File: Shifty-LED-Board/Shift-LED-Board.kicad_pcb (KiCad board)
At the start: 2 copper layers, 80 x 30 mm, 51 parts, among them U1 74AHCT595, U2 74AHCT595, U3 74AHCT595

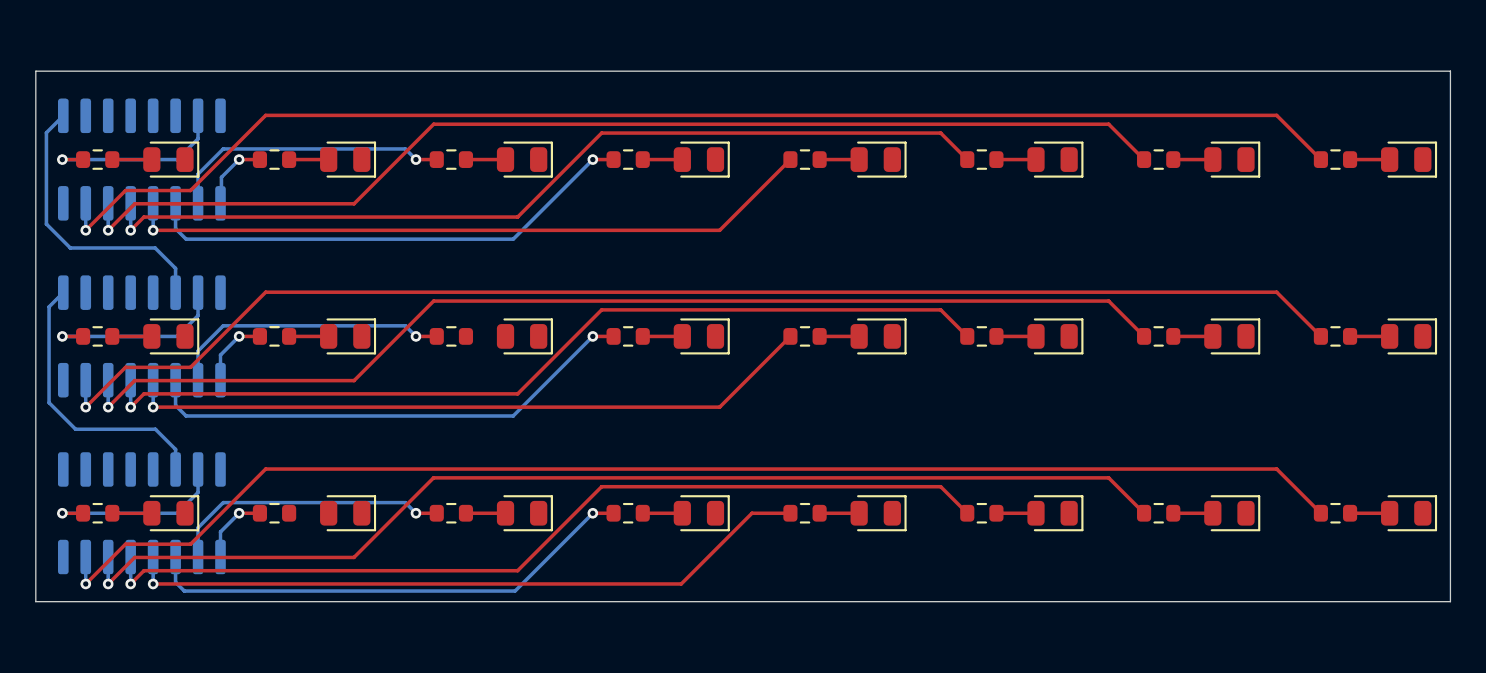
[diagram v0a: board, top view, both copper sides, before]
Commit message: added data routes on shfity board
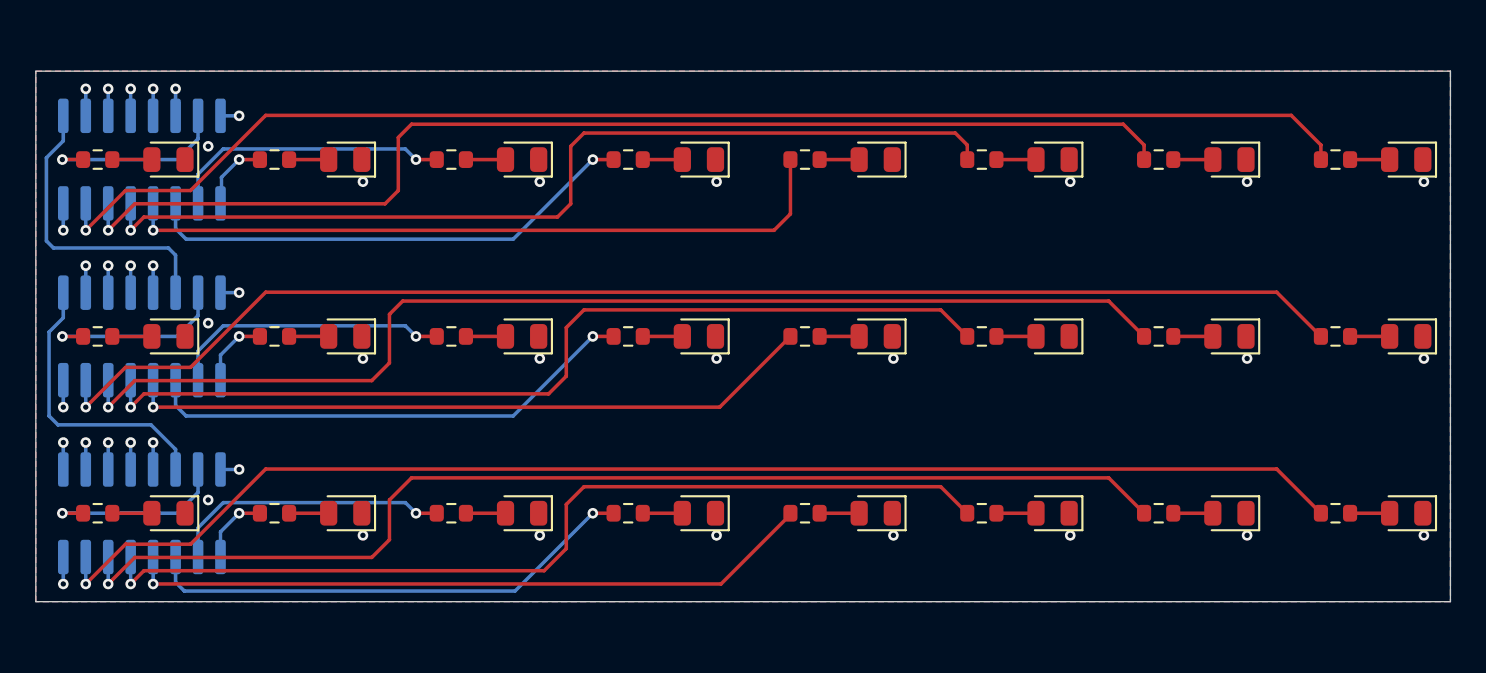
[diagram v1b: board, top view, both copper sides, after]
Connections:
- net /SER1 renamed /SER_IN
- U1 pad 10: unconnected-(U1-~{SRCLR}-Pad10) -> /SR_CLR
- U2 pad 10: unconnected-(U2-~{SRCLR}-Pad10) -> /SR_CLR
- U3 pad 10: unconnected-(U3-~{SRCLR}-Pad10) -> /SR_CLR
- U3 pad 9: unconnected-(U3-QH'-Pad9) -> /SER_OUT
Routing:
- net /SR_CLR: track 0.00 -> 25.6 mm, vias 0 -> 3
- net /SR_CLK: track 0.00 -> 25.6 mm, vias 0 -> 3
- net /RC_CLK: track 0.00 -> 25.6 mm, vias 0 -> 3
- net /OE: track 0.00 -> 25.6 mm, vias 0 -> 3
- net GND: track 0.00 -> 4.58 mm, vias 0 -> 25
- net /5V: track 0.00 -> 3.17 mm, vias 0 -> 3
- net Net-(U1-QF): track 51.7 -> 54.1 mm
- net Net-(U1-QG): track 63.4 -> 65.7 mm
- net Net-(D18-A): track 0.00 -> 2.24 mm
- net Net-(D11-A): track 0.00 -> 2.24 mm
- net Net-(U1-QE): track 39.4 -> 41.2 mm
- net Net-(U2-QG): track 63.4 -> 65.0 mm
- net Net-(U2-QF): track 51.7 -> 53.3 mm
- net /SER_OUT: track 0.00 -> 1.52 mm, vias 0 -> 1
- net /SER_IN: track 0.00 -> 1.52 mm, vias 0 -> 1
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- added copper zone on In2.Cu, net /5V
- added copper zone on B.Cu, net GND
- added copper zone on F.Cu, net GND
- added copper zone on In1.Cu, net GND
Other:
- copper layers 2 -> 4

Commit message: finished pcb layout and added fabrication files
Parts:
- added R25: 1k, Resistor_SMD:R_0603_1608Metric, F.Cu at (103.0, 43.5)
- added R26: 1k, Resistor_SMD:R_0603_1608Metric, F.Cu at (103.3, 63.5)
- added R27: 1k, Resistor_SMD:R_0603_1608Metric, F.Cu at (103.3, 53.5)
- added TP1: TestPoint, TestPoint:TestPoint_Pad_1.5x1.5mm, F.Cu at (96.2, 43.5)
- added TP10: TestPoint, TestPoint:TestPoint_Pad_1.5x1.5mm, F.Cu at (172.8, 43.5)
- added TP2: TestPoint, TestPoint:TestPoint_Pad_1.5x1.5mm, F.Cu at (172.8, 63.5)
- added TP3: TestPoint, TestPoint:TestPoint_Pad_1.5x1.5mm, F.Cu at (172.8, 53.5)
- added TP4: TestPoint, TestPoint:TestPoint_Pad_1.5x1.5mm, F.Cu at (172.8, 40.8)
- added TP5: TestPoint, TestPoint:TestPoint_Pad_1.5x1.5mm, F.Cu at (96.2, 71.2)
- added TP6: TestPoint, TestPoint:TestPoint_Pad_1.5x1.5mm, F.Cu at (96.2, 40.8)
- added TP7: TestPoint, TestPoint:TestPoint_Pad_1.5x1.5mm, F.Cu at (172.8, 71.2)
- added TP8: TestPoint, TestPoint:TestPoint_Pad_1.5x1.5mm, F.Cu at (96.2, 63.5)
- added TP9: TestPoint, TestPoint:TestPoint_Pad_1.5x1.5mm, F.Cu at (96.2, 53.5)
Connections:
- U1 pad 10: /SR_CLR -> unconnected-(U1-~{SRCLR}-Pad10)
- U2 pad 10: /SR_CLR -> unconnected-(U2-~{SRCLR}-Pad10)
- U3 pad 10: /SR_CLR -> unconnected-(U3-~{SRCLR}-Pad10)
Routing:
- net /SER_OUT: track 1.52 -> 106.0 mm, vias 1 -> 2
- net /RC_CLK: track 25.6 -> 117.3 mm, vias 3 -> 4
- net /SR_CLK: track 25.6 -> 109.0 mm, vias 3 -> 4
- net /SR_CLR: track 25.6 -> 0.00 mm, vias 3 -> 0
- net /5V: track 3.17 -> 12.9 mm, vias 3 -> 5
- net /SER_IN: track 1.52 -> 9.03 mm
- net /OE: track 25.6 -> 31.9 mm
- net GND: track 4.58 -> 8.97 mm, vias 25 -> 27
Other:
- board size 80 x 30 mm -> 80 x 34 mm

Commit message: added production files
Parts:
- R1, R10, R11, R12, R13, R14, R15, R16, R17, R18, R19, R2, R20, R21, R22, R23, R24, R3, R4, R5, R6, R7, R8, R9: value 330 -> 270
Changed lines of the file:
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@@
 			)
 		)
-		(property "Value" "330"
+		(property "Value" "270"
 			(at 0 1.43 0)
 			(layer "F.Fab")
@@
 			)
 		)
-		(property "Value" "330"
+		(property "Value" "270"
 			(at 0 1.43 0)
 			(layer "F.Fab")
@@
 			)
 		)
-		(property "Value" "330"
+		(property "Value" "270"
 			(at 0 1.43 0)
 			(layer "F.Fab")
@@
 			)
 		)
-		(property "Value" "330"
+		(property "Value" "270"
 			(at 0 1.43 0)
 			(layer "F.Fab")
@@
 			)
 		)
-		(property "Value" "330"
+		(property "Value" "270"
 			(at 0 1.43 0)
 			(layer "F.Fab")
@@
 			)
 		)
+		(property "LCSC Part #" "C23350"
+			(at 0 0 0)
+			(unlocked yes)
+			(layer "F.Fab")
+			(hide yes)
+			(effects
+				(font
+					(size 1 1)
+					(thickness 0.15)
+				)
+			)
+		)
 		(property ki_fp_filters "R_*")
 		(sheetname "/")
@@
 			)
 		)
-		(property "Value" "330"
+		(property "Value" "270"
 			(at 0 1.43 0)
 			(layer "F.Fab")
@@
 			)
 		)
-		(property "Value" "330"
+		(property "Value" "270"
 			(at 0 1.43 0)
 			(layer "F.Fab")
@@
 			)
 		)
-		(property "Value" "330"
+		(property "Value" "270"
 			(at 0 1.43 0)
 			(layer "F.Fab")
@@
 			)
 		)
+		(property "LCSC Part #" "C23350"
+			(at 0 0 0)
+			(unlocked yes)
+			(layer "F.Fab")
+			(hide yes)
+			(effects
+				(font
+					(size 1 1)
+					(thickness 0.15)
+				)
+			)
+		)
 		(property ki_fp_filters "R_*")
 		(sheetname "/")
@@
 			)
 		)
-		(property "Value" "330"
+		(property "Value" "270"
 			(at 0 1.43 0)
 			(layer "F.Fab")
@@
 			)
 		)
-		(property "Value" "330"
+		(property "Value" "270"
 			(at 0 1.43 0)
 			(layer "F.Fab")
@@
 			)
 		)
-		(property "Value" "330"
+		(property "Value" "270"
 			(at 0 1.43 0)
 			(layer "F.Fab")
@@
 			)
 		)
+		(property "LCSC Part #" "C34499"
+			(at 0 0 180)
+			(unlocked yes)
+			(layer "F.Fab")
+			(hide yes)
+			(effects
+				(font
+					(size 1 1)
+					(thickness 0.15)
+				)
+			)
+		)
 		(property ki_fp_filters "LED* LED_SMD:* LED_THT:*")
 		(sheetname "/")
@@
 			)
 		)
+		(property "LCSC Part #" "C34499"
+			(at 0 0 180)
+			(unlocked yes)
+			(layer "F.Fab")
+			(hide yes)
+			(effects
+				(font
+					(size 1 1)
+					(thickness 0.15)
+				)
+			)
+		)
 		(property ki_fp_filters "LED* LED_SMD:* LED_THT:*")
 		(sheetname "/")
@@
 			)
 		)
-		(property "Value" "330"
+		(property "Value" "270"
 			(at 0 1.43 0)
 			(layer "F.Fab")
@@
 			)
 		)
-		(property "Value" "330"
+		(property "Value" "270"
 			(at 0 1.43 0)
 			(layer "F.Fab")
@@
 			)
 		)
-		(property "Value" "330"
+		(property "Value" "270"
 			(at 0 1.43 0)
 			(layer "F.Fab")
@@
 			)
 		)
-		(property "Value" "330"
+		(property "Value" "270"
 			(at 0 1.43 0)
 			(layer "F.Fab")
@@
 			)
 		)
-		(property "Value" "330"
+		(property "Value" "270"
 			(at 0 1.43 0)
 			(layer "F.Fab")
@@
 			)
 		)
+		(property "LCSC Part #" "C23350"
+			(at 0 0 0)
+			(unlocked yes)
+			(layer "F.Fab")
+			(hide yes)
+			(effects
+				(font
+					(size 1 1)
+					(thickness 0.15)
+				)
+			)
+		)
 		(property ki_fp_filters "R_*")
 		(sheetname "/")
@@
 			)
 		)
-		(property "Value" "330"
+		(property "Value" "270"
 			(at 0 1.43 0)
 			(layer "F.Fab")
@@
 			)
 		)
-		(property "Value" "330"
+		(property "Value" "270"
 			(at 0 1.43 0)
 			(layer "F.Fab")
@@
 			)
 		)
-		(property "Value" "330"
+		(property "Value" "270"
 			(at 0 1.43 0)
 			(layer "F.Fab")
@@
 			)
 		)
-		(property "Value" "330"
+		(property "Value" "270"
 			(at 0 1.43 0)
 			(layer "F.Fab")
@@
 			)
 		)
-		(property "Value" "330"
+		(property "Value" "270"
 			(at 0 1.43 0)
 			(layer "F.Fab")
@@
 			)
 		)
-		(property "Value" "330"
+		(property "Value" "270"
 			(at 0 1.43 0)
 			(layer "F.Fab")
@@
 			)
 		)
-		(property "Value" "330"
+		(property "Value" "270"
 			(at 0 1.43 0)
 			(layer "F.Fab")
@@
 			)
 		)
-		(property "Value" "330"
+		(property "Value" "270"
 			(at 0 1.43 0)
 			(layer "F.Fab")
@@
 			(at 0 0 180)
 			(unlocked yes)
+			(layer "F.Fab")
+			(hide yes)
+			(effects
+				(font
+					(size 1 1)
+					(thickness 0.15)
+				)
+			)
+		)
+		(property "LCSC Part #" "C34499"
+			(at 0 0 180)
+			(unlocked yes)
